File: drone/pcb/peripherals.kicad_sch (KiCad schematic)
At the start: 23 parts, among them J2 Conn_02x11_Odd_Even, J3 Conn_01x04_MountingPin, SW1 SW_Push, SW3 SW_Push, U4 BMP388, U5 NRF24L01_Breakout, U7 BMI270, U8 HYCW110-TF10-180B

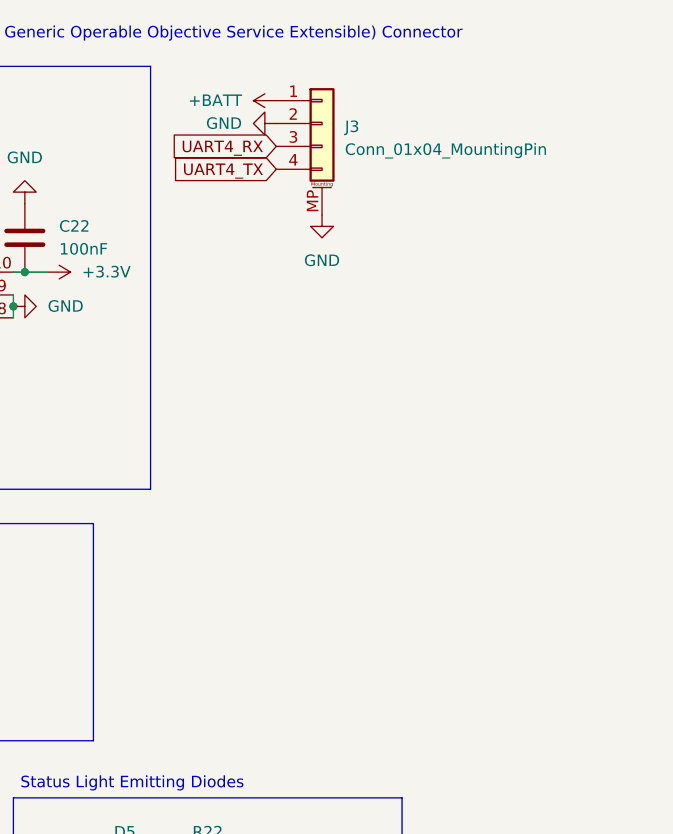
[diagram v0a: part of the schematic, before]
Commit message: [pcb] add JST FPV connector
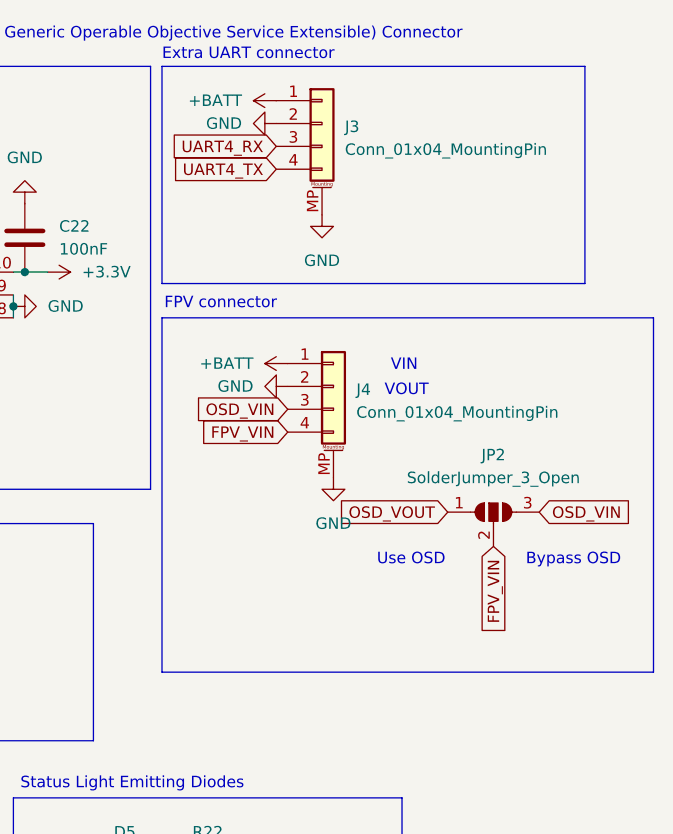
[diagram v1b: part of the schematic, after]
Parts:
- added J4: Conn_01x04_MountingPin, Connector_JST:JST_SH_BM04B-SRSS-TB_1x04-1MP_P1.00mm_Vertical, symbol Connector_Generic_MountingPin:Conn_01x04_MountingPin
- added JP2: SolderJumper_3_Open, Jumper:SolderJumper-3_P1.3mm_Open_RoundedPad1.0x1.5mm, symbol Jumper:SolderJumper_3_Open
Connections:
- net +BATT: now also J4.1 (Pin_1)
- net GND: now also J4.2 (Pin_2), J4.MP (MountPin)
- new net FPV_VIN: J4.4 (Pin_4), JP2.2 (C)
- new net OSD_VIN: J4.3 (Pin_3), JP2.3 (B)
- new net OSD_VOUT: JP2.1 (A)
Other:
- note added: "Bypass OSD"
- note added: "Extra UART connector"
- note added: "FPV connector"
- note added: "Use OSD"
- note added: "VIN"
- note added: "VOUT"
